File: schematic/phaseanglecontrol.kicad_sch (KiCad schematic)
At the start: 33 parts, among them J1 L_supply, J2 N_supply, J3 motor_housing, J4 N_motor, J5 L_motor, Q1 IRFP450, Q2 BS170, Q3 IRFR9310, Q4 IRFP450, U1 ATtiny26-16P, Y1 16 MHz

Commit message: Update schematic
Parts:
- R2, R3, R4: value 50 k -> 47 k
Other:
- note added: "TVS"
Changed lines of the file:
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@@
+		)
+	)
+	(text "TVS"
+		(exclude_from_sim no)
+		(at 161.798 38.354 0)
+		(effects
+			(font
+				(size 1.27 1.27)
+			)
 		)
 	)
@@
 			)
 		)
-		(property "Value" "50 k"
+		(property "Value" "47 k"
 			(at 165.1 53.3399 0)
 			(effects
@@
 			)
 		)
-		(property "Value" "50 k"
+		(property "Value" "47 k"
 			(at 139.7 35.5599 0)
 			(effects
@@
 			)
 		)
-		(property "Value" "50 k"
+		(property "Value" "47 k"
 			(at 142.24 59.6899 0)
 			(effects

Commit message: Update schematic
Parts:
- removed U1: ATtiny26-16P, Package_DIP:DIP-20_W7.62mm, symbol MCU_Microchip_ATtiny:ATtiny26-16P
- added U2: ATtiny861A-P, Package_DIP:DIP-20_W7.62mm, symbol MCU_Microchip_ATtiny:ATtiny861A-P
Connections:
- net +5V: now also U2.15 (AVCC), U2.5 (VCC)
- net GND: now also U2.16 (AGND), U2.6 (GND)
- net ISP/MISO: now also U2.2 (PB1)
- net ISP/MOSI: now also U2.1 (PB0)
- net ISP/RST: now also U2.10 (~{RESET}/PB7)
- net ISP/SCK: now also U2.3 (PB2)
- net debug: now also U2.9 (PB6)
- net mot_temp: now also U2.13 (PA5)
- net n_shutoff: now also U2.14 (PA4)
- net setpoint: now also U2.20 (PA0)
- net speedo_n: now also U2.11 (PA7)
- net speedo_p: now also U2.12 (PA6)
- net trig: now also U2.4 (PB3)
- net vsense: now also U2.19 (PA1)
- net at C6.1, Y1.2: now also U2.8 (XTAL2/PB5)
- net at C4.2, Y1.1: now also U2.7 (XTAL1/PB4)
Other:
- moved on the sheet: C1

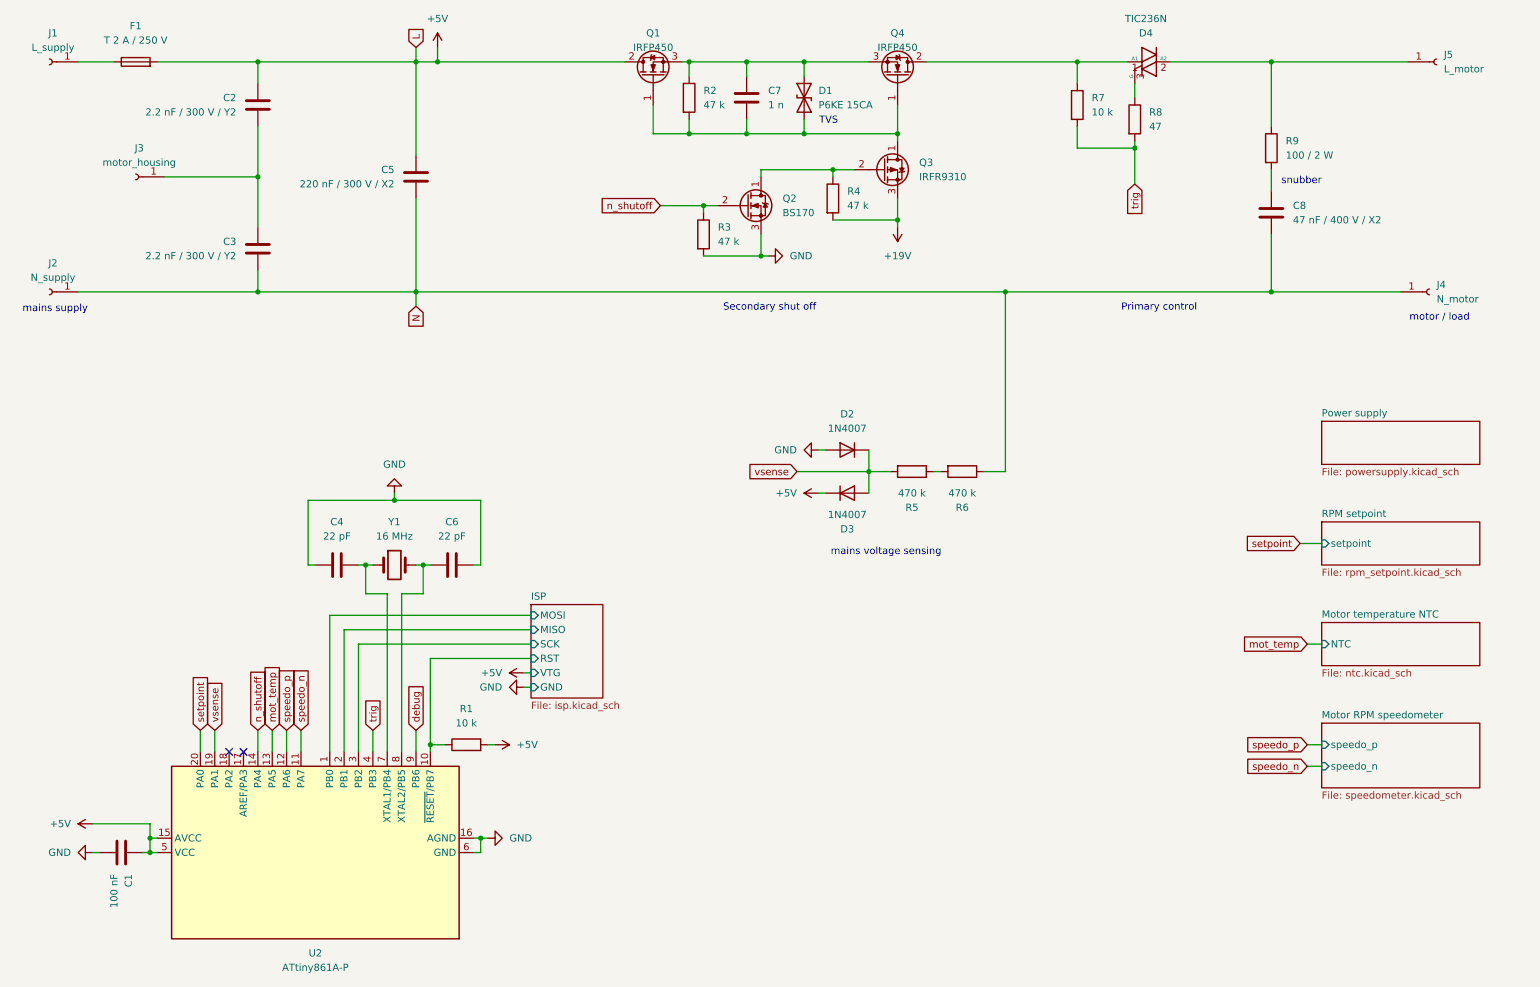
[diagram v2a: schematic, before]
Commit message: schematic: Add 2nd shutoff biasing
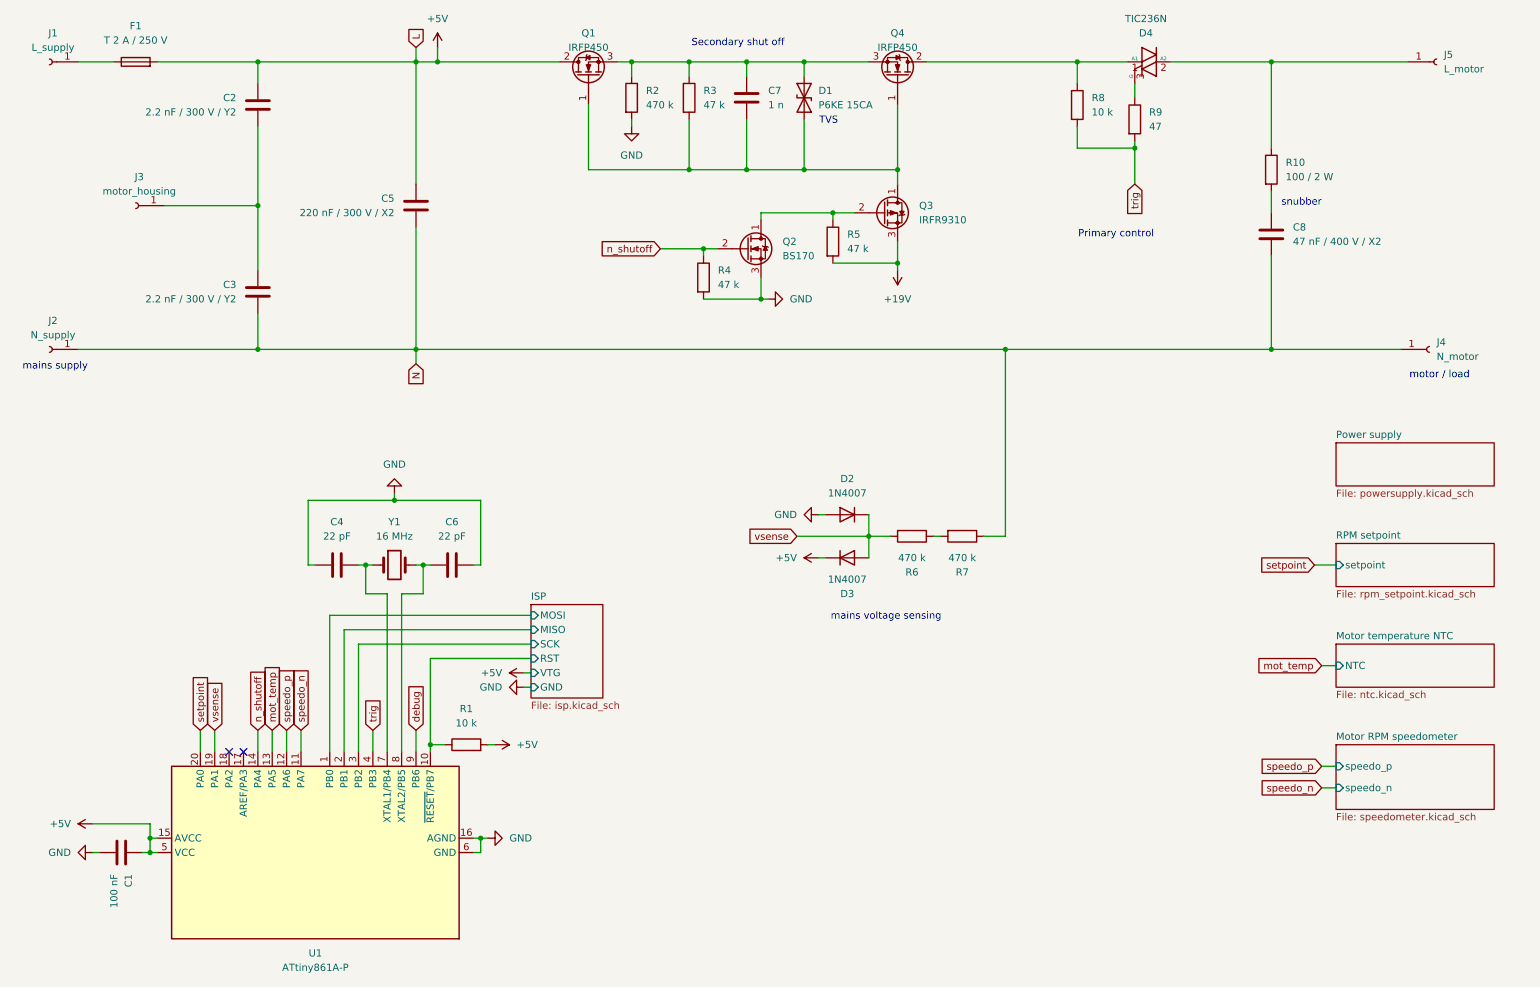
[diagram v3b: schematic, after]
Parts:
- added R2: 470 k, symbol Device:R
- renumbered R9 to R10, R2 to R3, R3 to R4, R4 to R5, R5 to R6, R6 to R7, R7 to R8, R8 to R9, U2 to U1
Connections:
- net GND: now also R2.2
- net at C7.1, D1.2 (A2), Q1.3 (S)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: now also R2.1
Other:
- moved on the sheet: C3, C5, C8, D2, D3, J2, J3, J4, Q1, Q2, Q3, R10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

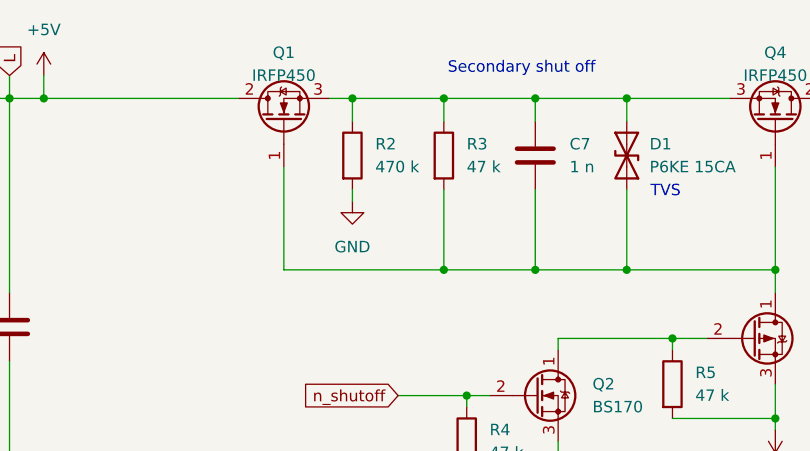
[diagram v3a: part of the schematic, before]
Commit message: schematic: Increase biasing
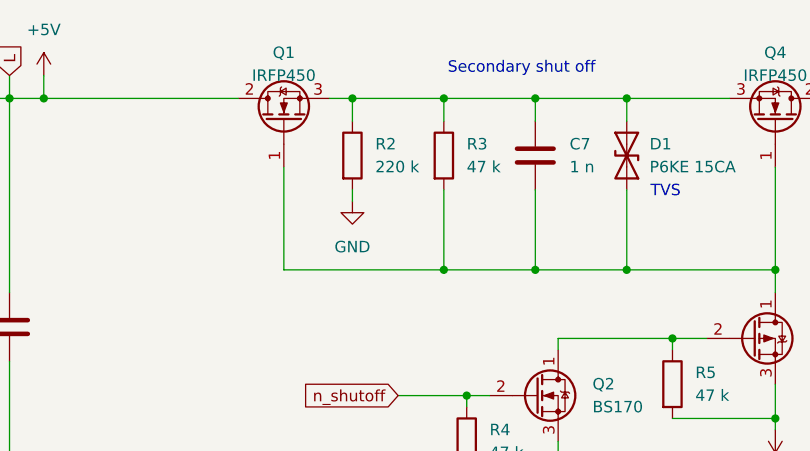
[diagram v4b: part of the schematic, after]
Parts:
- R2: value 470 k -> 220 k
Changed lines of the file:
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@@
 			)
 		)
-		(property "Value" "470 k"
+		(property "Value" "220 k"
 			(at 129.54 35.5599 0)
 			(effects

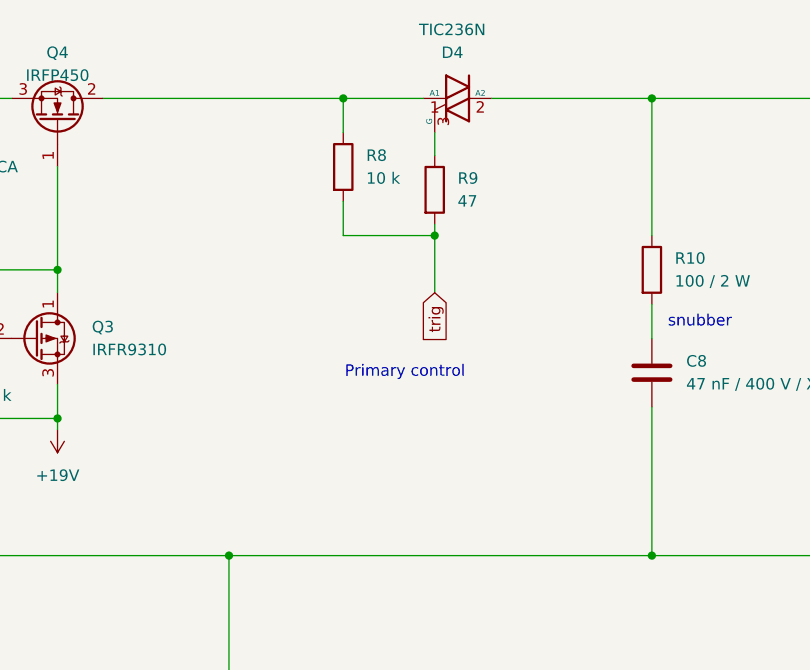
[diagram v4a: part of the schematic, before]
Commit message: Add TVS to tirac gate
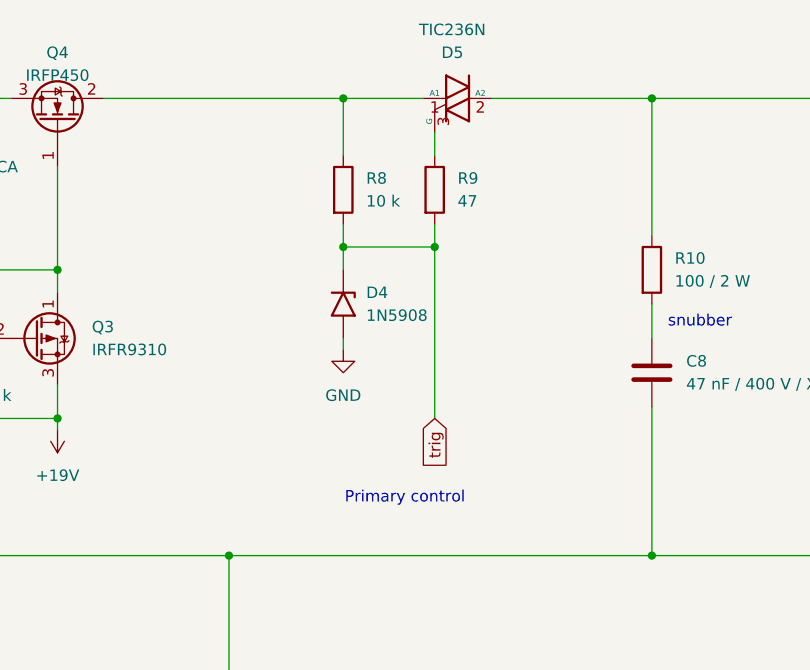
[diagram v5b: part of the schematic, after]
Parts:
- added D4: 1N5908, Diode_THT:D_DO-201AE_P15.24mm_Horizontal, symbol Diode:1N5908
- renumbered D4 to D5
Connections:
- net GND: now also D4.2 (A2)
- net trig: now also D4.1 (A1)
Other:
- moved on the sheet: R8
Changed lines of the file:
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@@
 	(text "Primary control"
 		(exclude_from_sim no)
-		(at 212.598 58.42 0)
+		(at 212.598 72.39 0)
 		(effects
 			(font
@@
 	)
 	(junction
+		(at 205.74 44.45)
+		(diameter 0)
+		(color 0 0 0 0)
+	)
+	(junction
 		(at 205.74 27.94)
 		(diameter 0)
@@
 	)
 	(junction
-		(at 215.9 43.18)
+		(at 92.71 27.94)
 		(diameter 0)
 		(color 0 0 0 0)
 	)
 	(junction
-		(at 92.71 27.94)
+		(at 215.9 44.45)
 		(diameter 0)
 		(color 0 0 0 0)
@@
 	(wire
 		(pts
-			(xy 215.9 43.18) (xy 215.9 49.53)
+			(xy 161.29 107.95) (xy 160.02 107.95)
 		)
 		(stroke
@@
 	(wire
 		(pts
-			(xy 161.29 107.95) (xy 160.02 107.95)
+			(xy 90.17 116.84) (xy 91.44 116.84)
 		)
 		(stroke
@@
 	(wire
 		(pts
-			(xy 90.17 116.84) (xy 91.44 116.84)
+			(xy 248.92 134.62) (xy 251.46 134.62)
 		)
 		(stroke
@@
 	(wire
 		(pts
-			(xy 248.92 134.62) (xy 251.46 134.62)
+			(xy 107.95 138.43) (xy 109.22 138.43)
 		)
 		(stroke
@@
 	(wire
 		(pts
-			(xy 107.95 138.43) (xy 109.22 138.43)
+			(xy 157.48 38.1) (xy 157.48 46.99)
 		)
 		(stroke
@@
 	(wire
 		(pts
-			(xy 157.48 38.1) (xy 157.48 46.99)
+			(xy 41.91 167.64) (xy 41.91 165.1)
 		)
 		(stroke
@@
 	(wire
 		(pts
-			(xy 41.91 167.64) (xy 41.91 165.1)
+			(xy 162.56 63.5) (xy 173.99 63.5)
 		)
 		(stroke
@@
 	(wire
 		(pts
-			(xy 162.56 63.5) (xy 173.99 63.5)
+			(xy 205.74 54.61) (xy 205.74 55.88)
 		)
 		(stroke
@@
 	(wire
 		(pts
-			(xy 157.48 27.94) (xy 168.91 27.94)
+			(xy 205.74 41.91) (xy 205.74 44.45)
 		)
 		(stroke
@@
 	(wire
 		(pts
-			(xy 172.72 111.76) (xy 168.91 111.76)
+			(xy 157.48 27.94) (xy 168.91 27.94)
 		)
 		(stroke
@@
 	(wire
 		(pts
-			(xy 90.17 121.92) (xy 86.36 121.92)
+			(xy 172.72 111.76) (xy 168.91 111.76)
 		)
 		(stroke
@@
 	(wire
 		(pts
-			(xy 168.91 111.76) (xy 156.21 111.76)
+			(xy 90.17 121.92) (xy 86.36 121.92)
 		)
 		(stroke
@@
 	(wire
 		(pts
-			(xy 240.03 62.23) (xy 240.03 78.74)
+			(xy 168.91 111.76) (xy 156.21 111.76)
 		)
 		(stroke
@@
 	(wire
 		(pts
-			(xy 68.58 146.05) (xy 68.58 149.86)
+			(xy 240.03 62.23) (xy 240.03 78.74)
 		)
 		(stroke
@@
 	(wire
 		(pts
-			(xy 43.18 27.94) (xy 60.96 27.94)
+			(xy 68.58 146.05) (xy 68.58 149.86)
 		)
 		(stroke
@@
 	(wire
 		(pts
-			(xy 205.74 39.37) (xy 205.74 43.18)
+			(xy 43.18 27.94) (xy 60.96 27.94)
 		)
 		(stroke
@@
 	(wire
 		(pts
-			(xy 205.74 43.18) (xy 215.9 43.18)
+			(xy 205.74 44.45) (xy 215.9 44.45)
 		)
 		(stroke
@@
 	(wire
 		(pts
-			(xy 215.9 41.91) (xy 215.9 43.18)
+			(xy 215.9 41.91) (xy 215.9 44.45)
 		)
 		(stroke
@@
 	(wire
 		(pts
+			(xy 205.74 44.45) (xy 205.74 46.99)
+		)
+		(stroke
+			(width 0)
+			(type default)
+		)
+	)
+	(wire
+		(pts
 			(xy 29.21 78.74) (xy 60.96 78.74)
 		)
@@
 	(wire
 		(pts
-			(xy 205.74 27.94) (xy 205.74 31.75)
+			(xy 205.74 27.94) (xy 205.74 34.29)
 		)
 		(stroke
@@
 	(wire
 		(pts
+			(xy 215.9 44.45) (xy 215.9 63.5)
+		)
+		(stroke
+			(width 0)
+			(type default)
+		)
+	)
+	(wire
+		(pts
 			(xy 60.96 78.74) (xy 88.9 78.74)
 		)
@@
 	(global_label "trig"
 		(shape input)
-		(at 215.9 49.53 270)
+		(at 215.9 63.5 270)
 		(fields_autoplaced yes)
 		(effects
@@
 		)
 		(property "Intersheetrefs" "${INTERSHEET_REFS}"
-			(at 215.9 55.7809 90)
+			(at 215.9 69.7509 90)
 			(effects
 				(font
@@
 	)
 	(symbol
+		(lib_id "Diode:1N5908")
+		(at 205.74 50.8 270)
+		(unit 1)
+		(exclude_from_sim no)
+		(in_bom yes)
+		(on_board yes)
+		(dnp no)
+		(fields_autoplaced yes)
+		(property "Reference" "D4"
+			(at 208.28 49.5299 90)
+			(effects
+				(font
+					(size 1.27 1.27)
+				)
+				(justify left)
+			)
+		)
+		(property "Value" "1N5908"
+			(at 208.28 52.0699 90)
+			(effects
+				(font
+					(size 1.27 1.27)
+				)
+				(justify left)
+			)
+		)
+		(property "Footprint" "Diode_THT:D_DO-201AE_P15.24mm_Horizontal"
+			(at 197.104 50.8 0)
+			(effects
+				(font
+					(size 1.27 1.27)
+				)
+				(hide yes)
+			)
+		)
+		(property "Datasheet" "https://www.st.com/resource/en/datasheet/1n5908.pdf"
+			(at 201.168 49.784 0)
+			(effects
+				(font
+					(size 1.27 1.27)
+				)
+				(hide yes)
+			)
+		)
+		(property "Description" "1500W (10/1000 μs) Unidirectional TVS Diode, VRM = 5V (IRM = 300 μA at 25°C), VBR = 6V, DO-201AE"
+			(at 199.136 50.8 0)
+			(effects
+				(font
+					(size 1.27 1.27)
+				)
+				(hide yes)
+			)
+		)
+		(pin "2"
+		)
+		(pin "1"
+		)
+		(instances
+			(project "phaseanglecontrol"
+				(path "/167e0419-9f88-4ea4-ae96-d03af9cd26b8"
+					(reference "D4")
+					(unit 1)
+				)
+			)
+		)
+	)
+	(symbol
 		(lib_id "Device:R")
 		(at 215.9 38.1 0)
@@
 	(symbol
 		(lib_id "Device:R")
-		(at 205.74 35.56 0)
+		(at 205.74 38.1 0)
 		(unit 1)
 		(exclude_from_sim no)
@@
 		(fields_autoplaced yes)
 		(property "Reference" "R8"
-			(at 208.28 34.2899 0)
+			(at 208.28 36.8299 0)
 			(effects
 				(font
@@
 		)
 		(property "Value" "10 k"
-			(at 208.28 36.8299 0)
+			(at 208.28 39.3699 0)
 			(effects
 				(font
@@
 		)
 		(property "Footprint" ""
-			(at 203.962 35.56 90)
+			(at 203.962 38.1 90)
 			(effects
 				(font
@@
 		)
 		(property "Datasheet" "~"
-			(at 205.74 35.56 0)
+			(at 205.74 38.1 0)
 			(effects
 				(font
@@
 		)
 		(property "Description" "Resistor"
-			(at 205.74 35.56 0)
+			(at 205.74 38.1 0)
 			(effects
 				(font
@@
 		(on_board yes)
 		(dnp no)
-		(property "Reference" "D4"
+		(property "Reference" "D5"
 			(at 217.8685 22.86 90)
 			(effects
@@
 			(project ""
 				(path "/167e0419-9f88-4ea4-ae96-d03af9cd26b8"
-					(reference "D4")
+					(reference "D5")
 					(unit 1)
 				)
@@
 					(unit 1)
 				)
+			)
+		)
+	)
+	(symbol
+		(lib_id "power:GND")
+		(at 205.74 55.88 0)
+		(unit 1)
+		(exclude_from_sim no)
+		(in_bom yes)
+		(on_board yes)
+		(dnp no)
+		(fields_autoplaced yes)
+		(property "Reference" "#PWR014"
+			(at 205.74 62.23 0)
+			(effects
+				(font
+					(size 1.27 1.27)
+				)
+				(hide yes)
+			)
+		)
+		(property "Value" "GND"
+			(at 205.74 60.96 0)
+			(effects
+				(font
+					(size 1.27 1.27)
+				)
+			)
+		)
+		(property "Footprint" ""
+			(at 205.74 55.88 0)
+			(effects
+				(font
+					(size 1.27 1.27)
+				)
+				(hide yes)
+			)
+		)
+		(property "Datasheet" ""
+			(at 205.74 55.88 0)
+			(effects
+				(font
+					(size 1.27 1.27)
+				)
+				(hide yes)
+			)
+		)
+		(property "Description" "Power symbol creates a global label with name \"GND\" , ground"
+			(at 205.74 55.88 0)
+			(effects
+				(font
+					(size 1.27 1.27)
+				)
+				(hide yes)
+			)
+		)
+		(pin "1"
+		)
+		(instances
+			(project "phaseanglecontrol"
+				(path "/167e0419-9f88-4ea4-ae96-d03af9cd26b8"
+					(reference "#PWR014")
+					(unit 1)
+				)
